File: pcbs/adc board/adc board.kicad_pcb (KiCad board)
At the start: 2 copper layers, 28 x 25 mm, 15 parts, among them IC1 ADS122C04IPWR, J1 Screw_Terminal_01x06, J5 Screw_Terminal_01x07

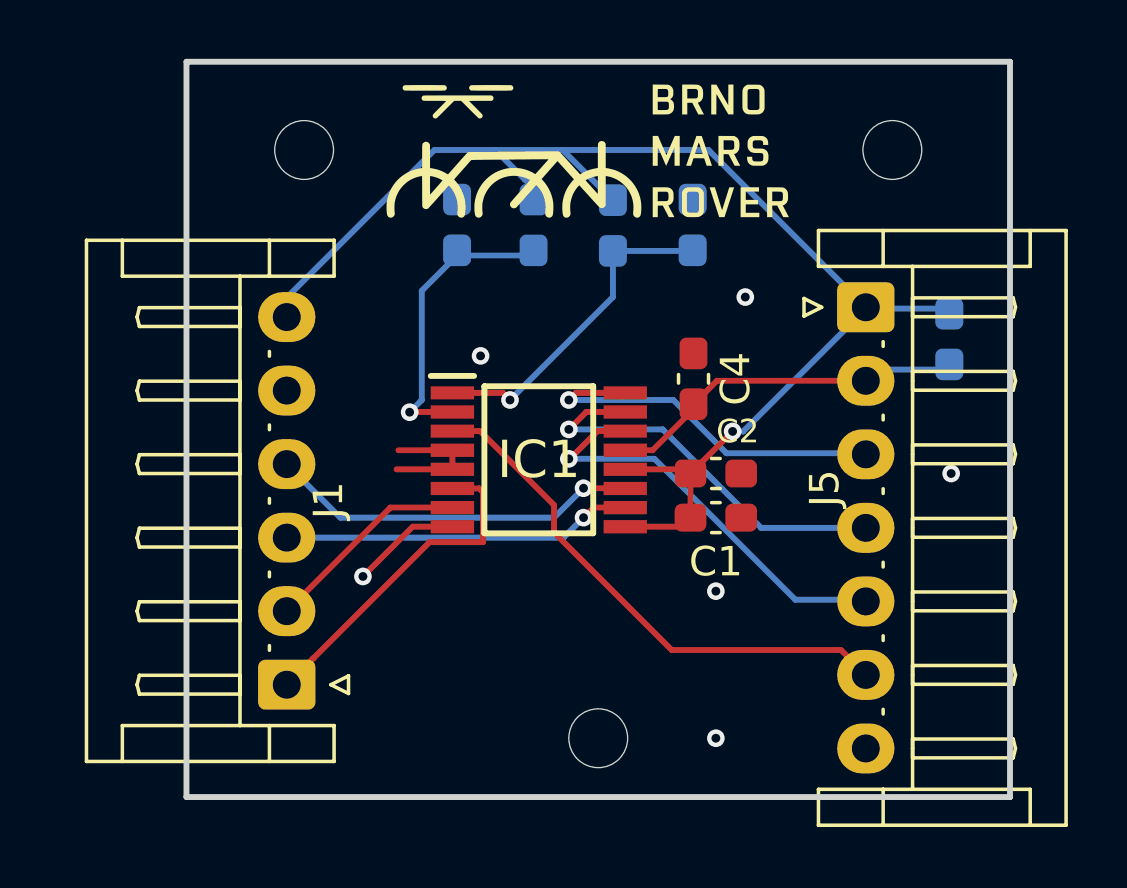
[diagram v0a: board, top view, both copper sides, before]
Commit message: adc board scaled down
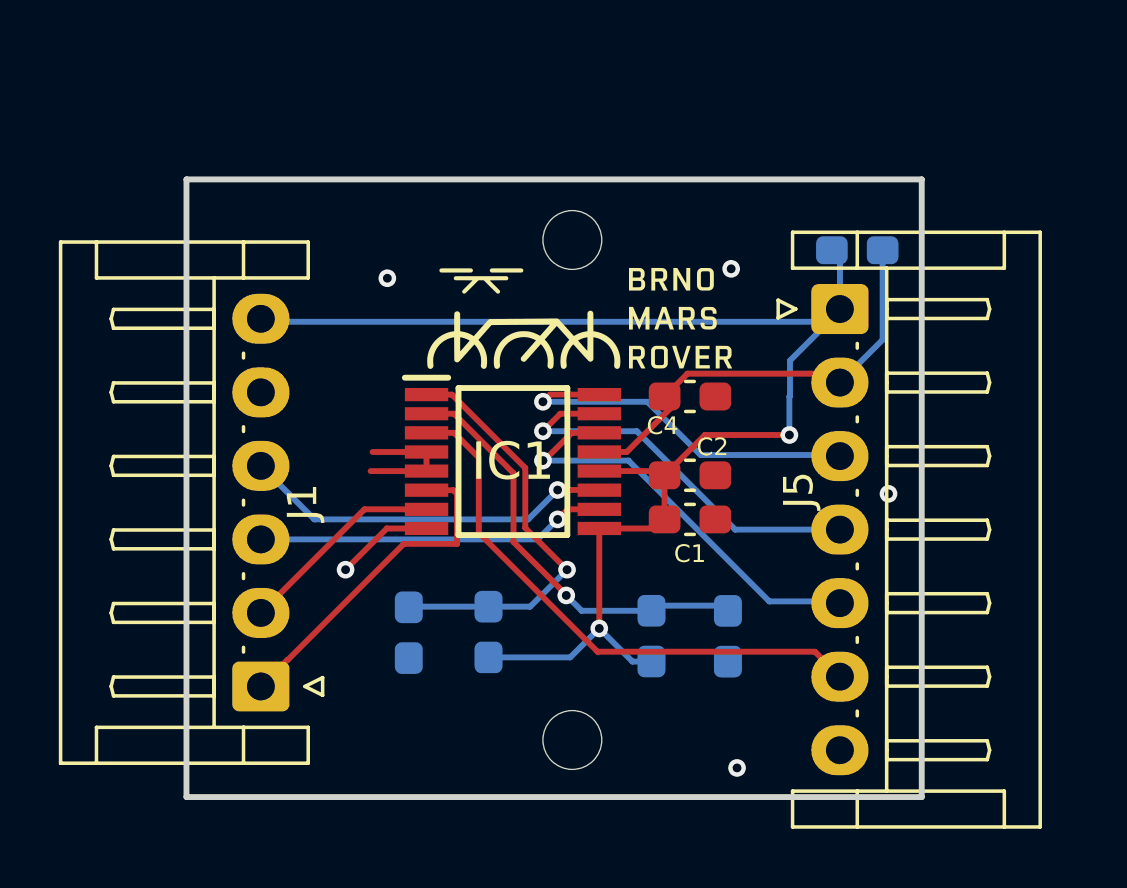
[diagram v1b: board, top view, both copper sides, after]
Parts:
- removed the REF** at (14.0, 13.0)
- moved solderable_connection4 16.9 mm to (17.6, 29.4), turned to 90 degrees
- moved solderable_connection1 16.7 mm to (28.4, 29.5), turned to 90 degrees
- moved solderable_connection2 14.5 mm to (25.8, 29.5), turned to 90 degrees
- moved solderable_connection3 14.5 mm to (20.3, 29.4), turned to 90 degrees
- moved REF** 11.3 mm to (23.1, 16.1)
- moved G*** 5.68 mm to (23.5, 18.8)
- moved solderable_connection0 4.35 mm to (32.8, 16.4), turned to 180 degrees
- moved J1 0.88 mm to (12.5, 31.2)
- moved IC1 0.88 mm to (21.1, 23.6)
- moved REF** 0.88 mm to (23.1, 33.1)
- moved C1 0.88 mm to (27.1, 25.6)
- moved C2 0.88 mm to (27.1, 24.1)
- moved J5 0.88 mm to (32.2, 18.4)
- moved C4 0.61 mm to (27.1, 21.4), turned to 180 degrees
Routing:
- net Net-(IC1-A1): track 10.1 -> 14.8 mm
- net Net-(IC1-A0): track 11.3 -> 14.3 mm
- net +3.3V: track 12.4 -> 15.2 mm
- net +5V: track 47.0 -> 49.3 mm, vias 1 -> 2
- net neg_RESET: track 18.0 -> 19.0 mm
- net GND: track 8.84 -> 8.43 mm, vias 6 -> 5
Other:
- board size 28 x 25 mm -> 25 x 21 mm

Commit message: fix drc errors and recreate grbl files
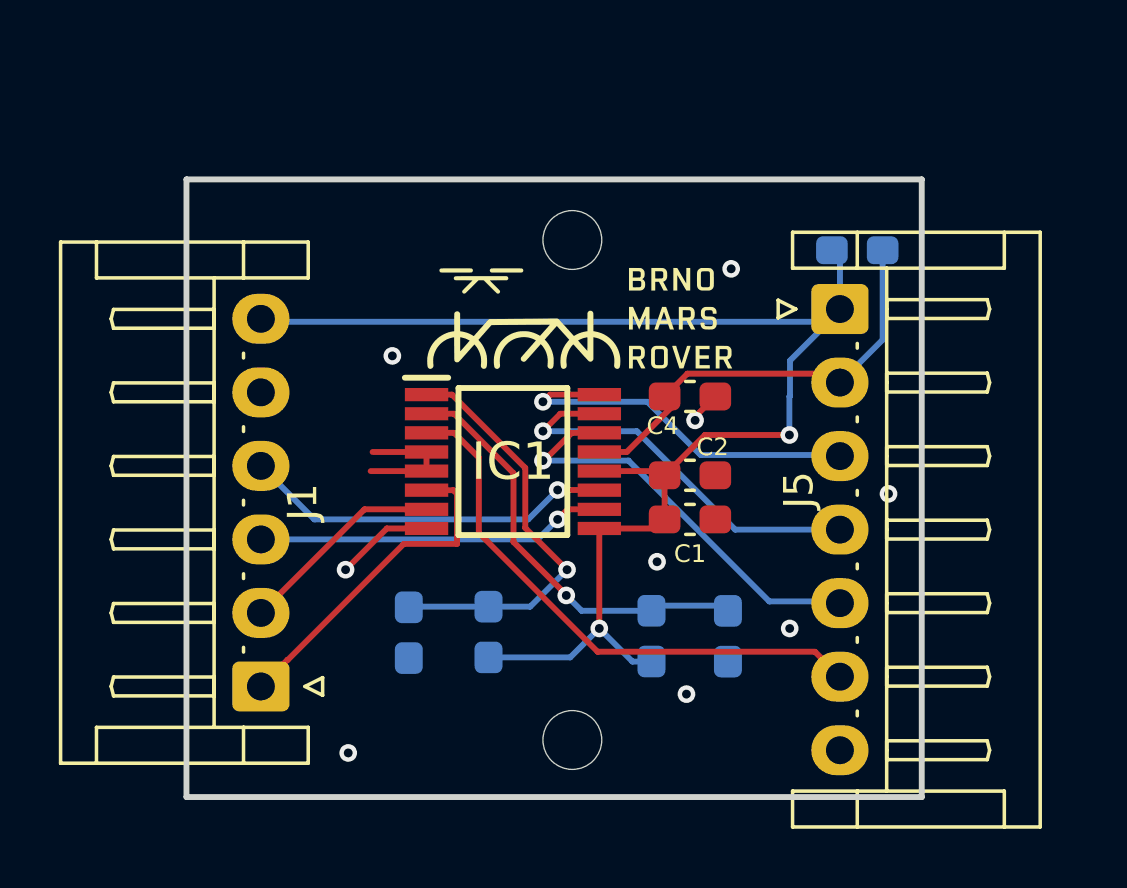
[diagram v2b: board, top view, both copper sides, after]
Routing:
- net GND: track 8.43 -> 9.53 mm, vias 5 -> 9
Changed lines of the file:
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@@
+	)
+	(segment
+		(start 27.293168 22.19178)
+		(end 27.293168 22.069332)
+		(width 0.2)
+		(layer "F.Cu")
+		(net 1)
 	)
 	(segment
@@
 	)
 	(segment
+		(start 27.293168 22.069332)
+		(end 27.9825 21.38)
+		(width 0.2)
+		(layer "F.Cu")
+		(net 1)
+	)
+	(segment
 		(start 18.162 23.2675)
 		(end 18.162 23.9175)
@@
 	)
 	(via
-		(at 16.83 17.36)
+		(at 17 20)
+		(size 0.6)
+		(drill 0.3)
+		(layers "F.Cu" "B.Cu")
+		(net 1)
+	)
+	(via
+		(at 27.293168 22.19178)
+		(size 0.6)
+		(drill 0.3)
+		(layers "F.Cu" "B.Cu")
+		(net 1)
+	)
+	(via
+		(at 30.510534 29.268248)
+		(size 0.6)
+		(drill 0.3)
+		(layers "F.Cu" "B.Cu")
+		(net 1)
+	)
+	(via
+		(at 26 27)
 		(size 0.6)
 		(drill 0.3)
@@
 	)
 	(via
-		(at 28.72 34.01)
+		(at 27 31.5)
 		(size 0.6)
 		(drill 0.3)
@@
 		(size 0.6)
 		(drill 0.3)
+		(layers "F.Cu" "B.Cu")
+		(net 1)
+	)
+	(via
+		(at 15.5 33.5)
+		(size 0.6)
+		(drill 0.3)

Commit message: 3.3 voltage level to address selection
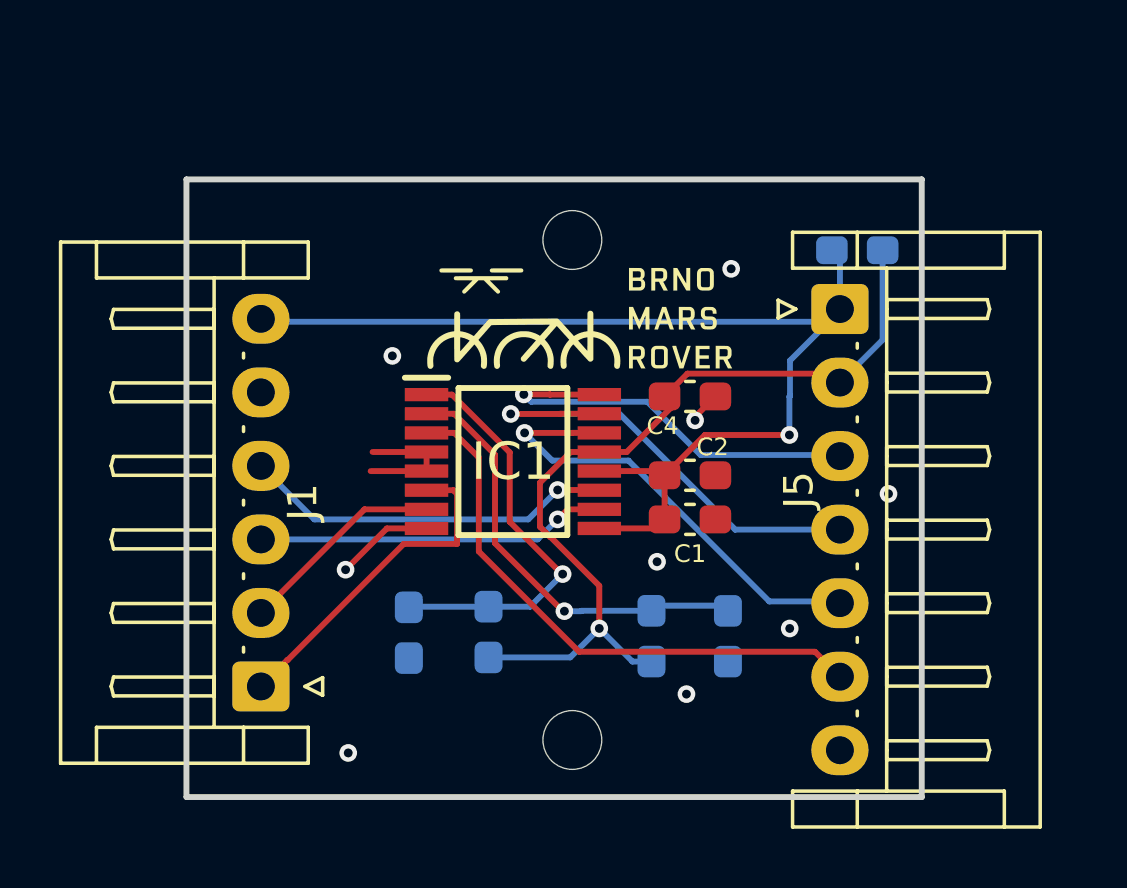
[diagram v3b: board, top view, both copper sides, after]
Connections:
- solderable_connection2 pad 1: +5V -> +3.3V
- solderable_connection3 pad 1: +5V -> +3.3V
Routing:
- net +3.3V: track 15.2 -> 30.4 mm, vias 0 -> 1
- net +5V: track 49.3 -> 39.1 mm, vias 2 -> 1
- net SDA: track 13.6 -> 15.8 mm
- net SCL: track 13.1 -> 14.4 mm
- net neg_DRDY: track 14.4 -> 15.7 mm
